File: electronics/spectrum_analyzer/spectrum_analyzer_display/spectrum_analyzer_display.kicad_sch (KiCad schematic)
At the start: 16 parts, among them J4 Conn_01x10_Pin, J5 Conn_01x14_Pin

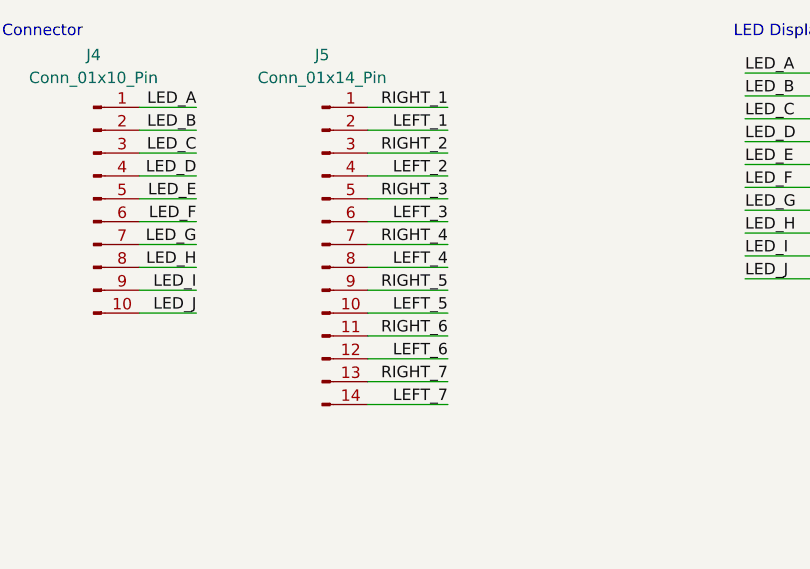
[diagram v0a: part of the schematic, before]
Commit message: feat: change pcb layout and enclosure design
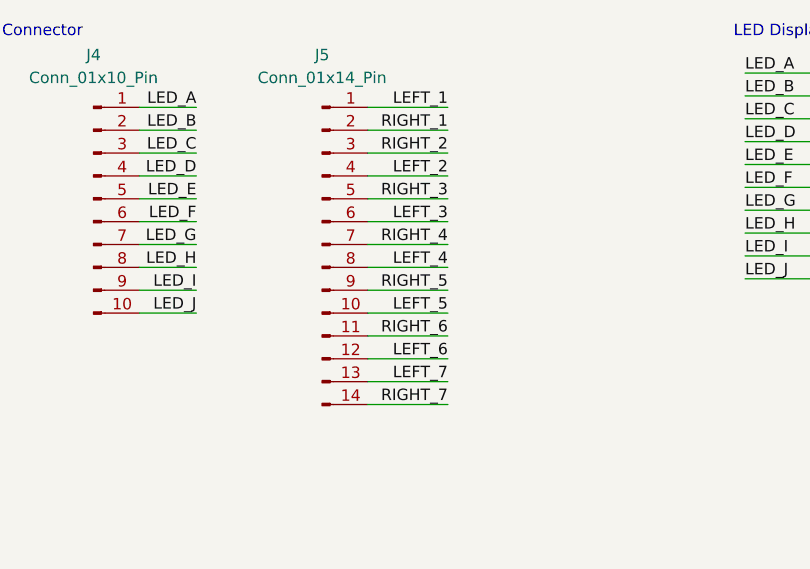
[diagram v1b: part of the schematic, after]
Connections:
- net LEFT_1: now also J5.1 (Pin_1); no longer J5.2 (Pin_2)
- net LEFT_7: now also J5.13 (Pin_13); no longer J5.14 (Pin_14)
- net RIGHT_1: now also J5.2 (Pin_2); no longer J5.1 (Pin_1)
- net RIGHT_7: now also J5.14 (Pin_14); no longer J5.13 (Pin_13)
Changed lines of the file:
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@@
     (effects (font (size 1.27 1.27)) (justify left bottom))
   )
-  (label "RIGHT_1" (at 87.63 35.56 180) (fields_autoplaced)
+  (label "LEFT_1" (at 87.63 35.56 180) (fields_autoplaced)
     (effects (font (size 1.27 1.27)) (justify right bottom))
   )
@@
     (effects (font (size 1.27 1.27)) (justify left bottom))
   )
-  (label "RIGHT_7" (at 87.63 66.04 180) (fields_autoplaced)
+  (label "LEFT_7" (at 87.63 66.04 180) (fields_autoplaced)
     (effects (font (size 1.27 1.27)) (justify right bottom))
   )
@@
     (effects (font (size 1.27 1.27)) (justify left bottom))
   )
-  (label "LEFT_1" (at 87.63 38.1 180) (fields_autoplaced)
+  (label "RIGHT_1" (at 87.63 38.1 180) (fields_autoplaced)
     (effects (font (size 1.27 1.27)) (justify right bottom))
   )
@@
     (effects (font (size 1.27 1.27)) (justify right bottom))
   )
-  (label "LEFT_7" (at 87.63 68.58 180) (fields_autoplaced)
-    (effects (font (size 1.27 1.27)) (justify right bottom))
-  )
+  (label "RIGHT_7" (at 87.63 68.58 180) (fields_autoplaced)
+    (effects (font (size 1.27 1.27)) (justify right bottom))
+  )
